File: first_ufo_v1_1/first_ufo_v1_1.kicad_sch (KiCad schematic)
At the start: 71 parts, among them J2 Barrel_Jack_Switch, Q1 2N3904, SW1 SMTS-102, SW2 SMTS-102, SW3 SMTS-102, U1 40106, U3 LM358

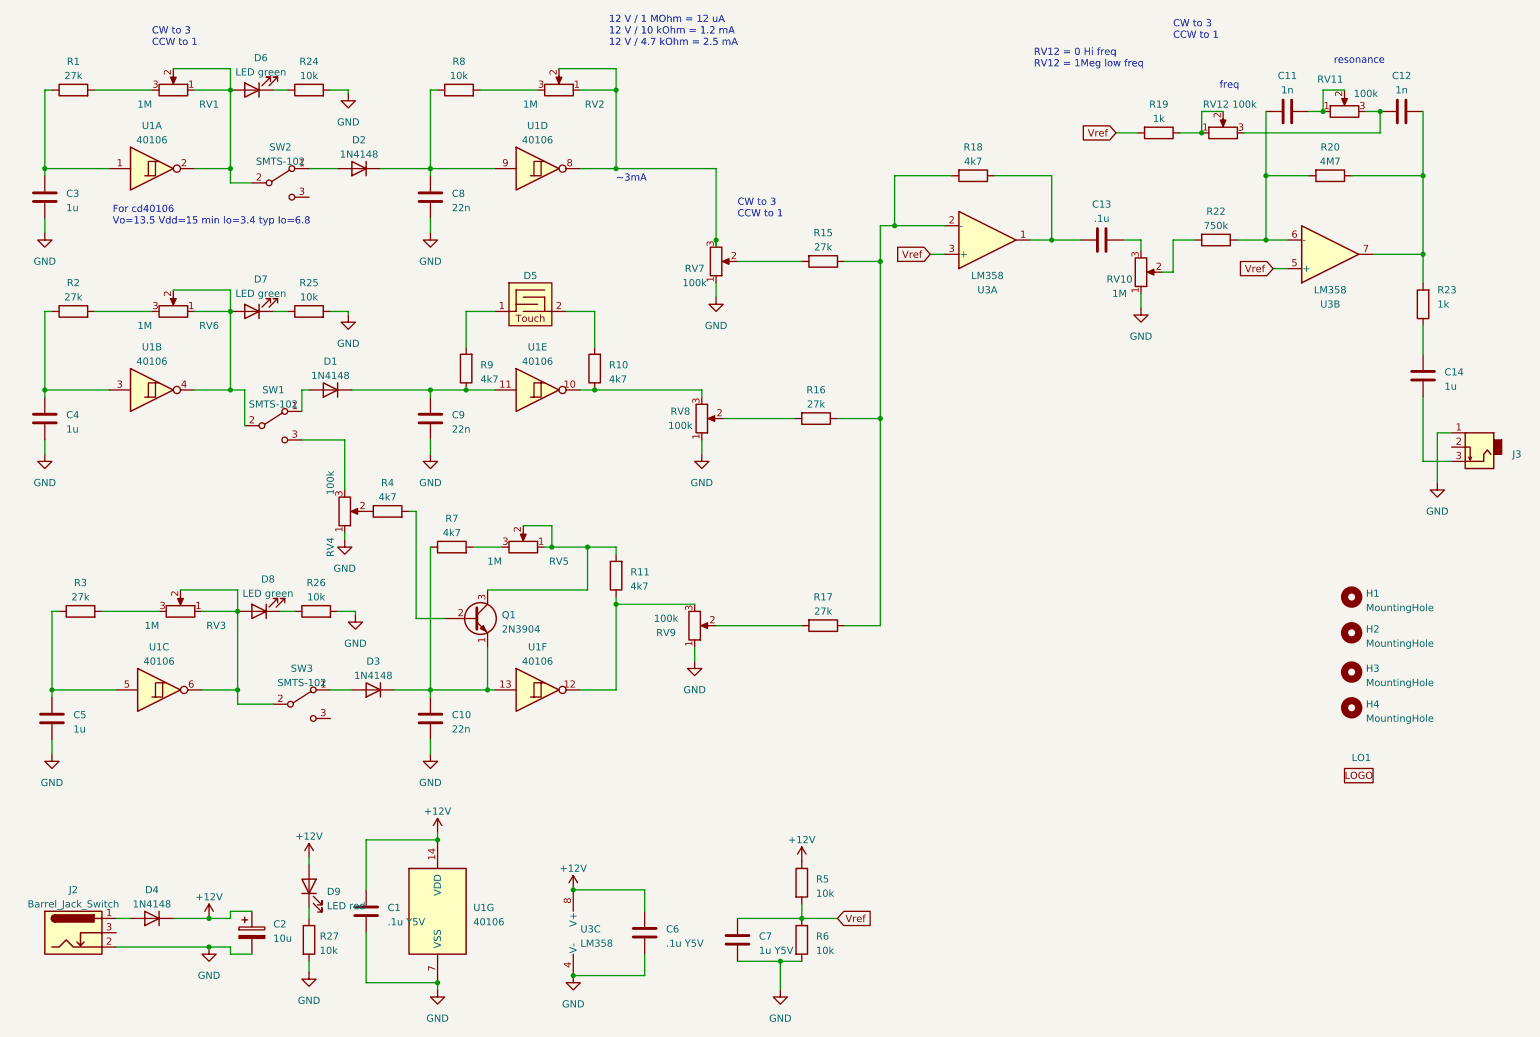
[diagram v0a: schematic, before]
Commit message: change R18 to 1k. that needs for increase dynamic range in case of all oscs in high volume level
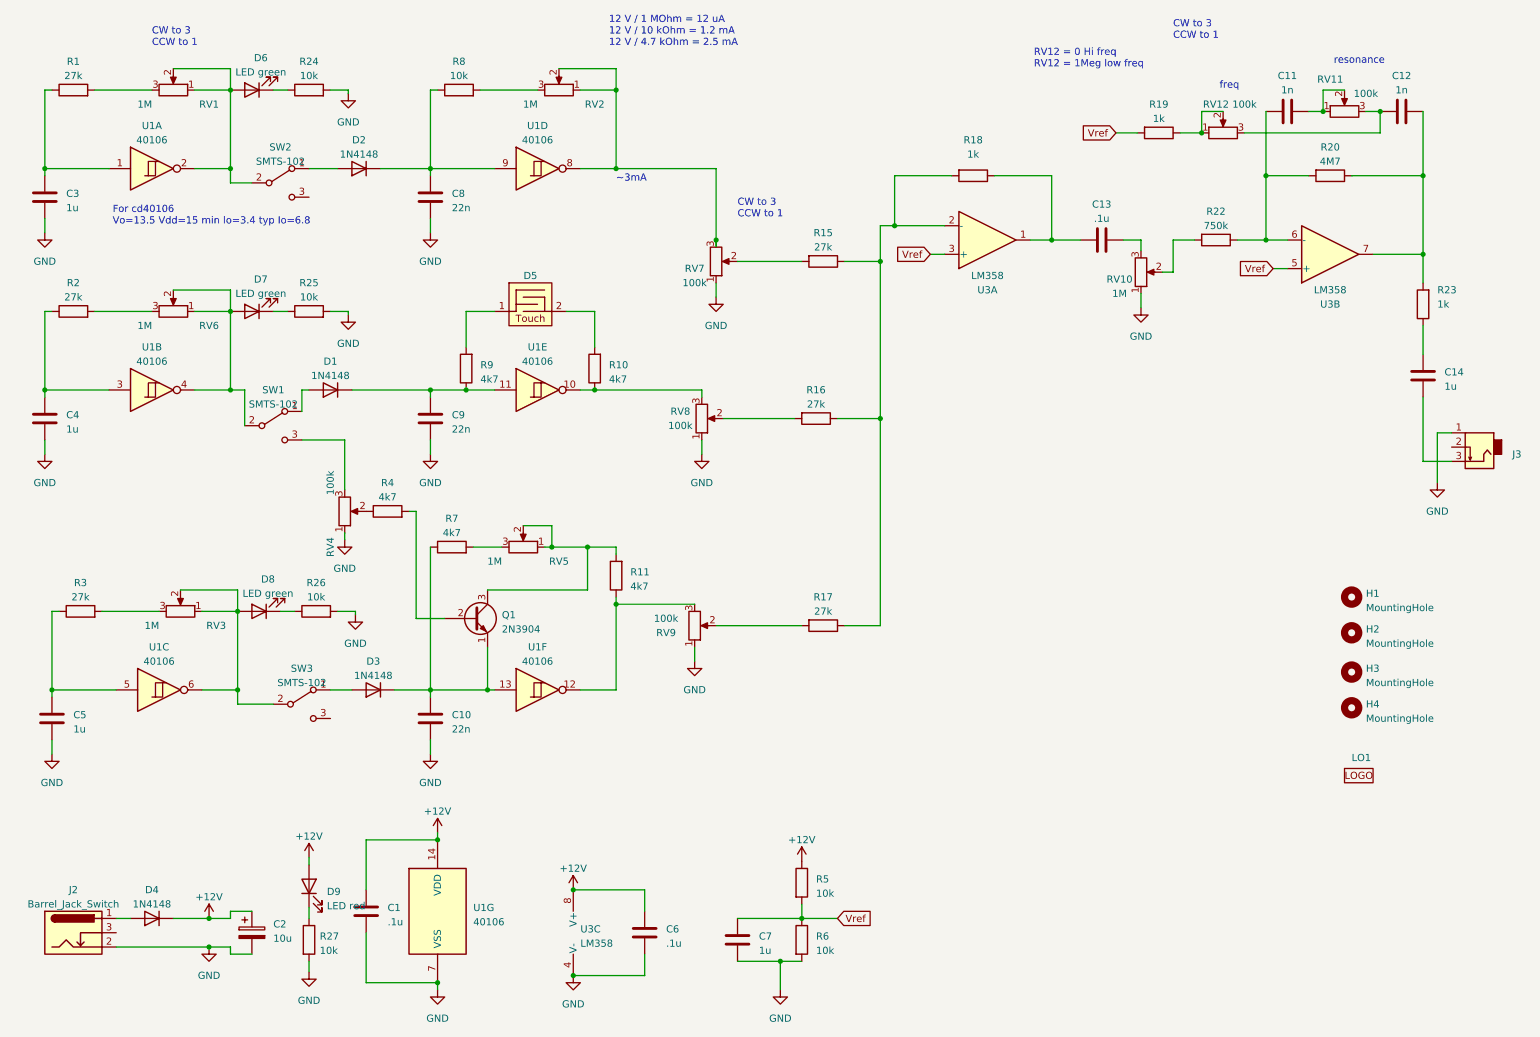
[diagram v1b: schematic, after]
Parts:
- C1, C6: value .1u Y5V -> .1u
- C7: value 1u Y5V -> 1u
- R18: value 4k7 -> 1k
